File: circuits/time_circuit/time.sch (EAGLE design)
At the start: 6 parts, among them Y2 32.768kHz

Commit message: Integrated wires to main schematic
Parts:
- added GND: SE13, solpad:SE13
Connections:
- net VCC renamed VDD
- net GND: now also GND.MP
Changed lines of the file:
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@@
 <parts>
 <part name="DS1307" library="ds1307_pcf8583" deviceset="DS1307" device=""/>
-<part name="GND1" library="supply1" deviceset="GND" device=""/>
-<part name="GND2" library="supply1" deviceset="GND" device=""/>
-<part name="P+1" library="supply1" deviceset="VCC" device=""/>
 <part name="R1" library="SparkFun-Resistors" deviceset="10KOHM-1/10W-1%(0603)" device="0603" value="10K"/>
 <part name="R2" library="SparkFun-Resistors" deviceset="10KOHM-1/10W-1%(0603)" device="0603" value="10K"/>
-<part name="P+2" library="supply1" deviceset="VCC" device=""/>
-<part name="P+3" library="supply1" deviceset="VCC" device=""/>
 <part name="SCL_RTC" library="solpad" deviceset="SE13" device=""/>
 <part name="SDA_RTC" library="solpad" deviceset="SE13" device=""/>
 <part name="Y2" library="SparkFun-FreqCtrl" deviceset="CRYSTAL" device="TC26H" value="32.768kHz"/>
+<part name="GND" library="solpad" deviceset="SE13" device=""/>
+<part name="GND2" library="supply1" deviceset="GND" device=""/>
+<part name="VDD1" library="supply1" deviceset="VDD" device=""/>
+<part name="VDD2" library="supply1" deviceset="VDD" device=""/>
+<part name="VDD3" library="supply1" deviceset="VDD" device=""/>
 </parts>
 <sheets>
@@
 <instances>
 <instance part="DS1307" gate="G$1" x="48.26" y="60.96"/>
-<instance part="GND1" gate="1" x="33.02" y="53.34" rot="R270"/>
-<instance part="GND2" gate="1" x="63.5" y="53.34" rot="R90"/>
-<instance part="P+1" gate="VCC" x="30.48" y="68.58" rot="R90"/>
 <instance part="R1" gate="G$1" x="60.96" y="76.2" rot="R90"/>
 <instance part="R2" gate="G$1" x="88.9" y="68.58" rot="R90"/>
-<instance part="P+2" gate="VCC" x="60.96" y="83.82"/>
-<instance part="P+3" gate="VCC" x="88.9" y="76.2"/>
 <instance part="SCL_RTC" gate="1" x="73.66" y="68.58" rot="R270"/>
 <instance part="SDA_RTC" gate="1" x="96.52" y="63.5" rot="R270"/>
 <instance part="Y2" gate="G$1" x="22.86" y="60.96" rot="R90"/>
+<instance part="GND" gate="1" x="71.12" y="53.34" rot="R270"/>
+<instance part="GND2" gate="1" x="33.02" y="53.34" rot="R270"/>
+<instance part="VDD1" gate="G$1" x="33.02" y="71.12"/>
+<instance part="VDD2" gate="G$1" x="60.96" y="83.82"/>
+<instance part="VDD3" gate="G$1" x="88.9" y="76.2"/>
 </instances>
 <busses>
 </busses>
 <nets>
-<net name="GND" class="0">
-<segment>
-<pinref part="DS1307" gate="G$1" pin="GND"/>
-<pinref part="GND1" gate="1" pin="GND"/>
-<wire x1="35.56" y1="53.34" x2="38.1" y2="53.34" width="0.1524" layer="91"/>
-</segment>
-<segment>
-<pinref part="DS1307" gate="G$1" pin="VBAT"/>
-<pinref part="GND2" gate="1" pin="GND"/>
-</segment>
-</net>
-<net name="VCC" class="0">
-<segment>
-<pinref part="DS1307" gate="G$1" pin="VCC"/>
-<pinref part="P+1" gate="VCC" pin="VCC"/>
-<wire x1="33.02" y1="68.58" x2="38.1" y2="68.58" width="0.1524" layer="91"/>
-</segment>
-<segment>
-<pinref part="R1" gate="G$1" pin="2"/>
-<pinref part="P+2" gate="VCC" pin="VCC"/>
-</segment>
-<segment>
-<pinref part="R2" gate="G$1" pin="2"/>
-<pinref part="P+3" gate="VCC" pin="VCC"/>
-</segment>
-</net>
 <net name="N$1" class="0">
 <segment>
@@
 </segment>
 </net>
+<net name="GND" class="0">
+<segment>
+<pinref part="DS1307" gate="G$1" pin="GND"/>
+<pinref part="GND2" gate="1" pin="GND"/>
+<wire x1="35.56" y1="53.34" x2="38.1" y2="53.34" width="0.1524" layer="91"/>
+<pinref part="DS1307" gate="G$1" pin="VBAT"/>
+<wire x1="63.5" y1="53.34" x2="60.96" y2="53.34" width="0.1524" layer="91"/>
+<wire x1="38.1" y1="45.72" x2="63.5" y2="45.72" width="0.1524" layer="91"/>
+<wire x1="63.5" y1="45.72" x2="63.5" y2="53.34" width="0.1524" layer="91"/>
+<wire x1="63.5" y1="53.34" x2="68.58" y2="53.34" width="0.1524" layer="91"/>
+<pinref part="GND" gate="1" pin="MP"/>
+<wire x1="38.1" y1="45.72" x2="38.1" y2="53.34" width="0.1524" layer="91"/>
+</segment>
+</net>
+<net name="VDD" class="0">
+<segment>
+<pinref part="DS1307" gate="G$1" pin="VCC"/>
+<wire x1="33.02" y1="68.58" x2="38.1" y2="68.58" width="0.1524" layer="91"/>
+<pinref part="VDD1" gate="G$1" pin="VDD"/>
+</segment>
+<segment>
+<pinref part="R1" gate="G$1" pin="2"/>
+<pinref part="VDD2" gate="G$1" pin="VDD"/>
+</segment>
+<segment>
+<pinref part="R2" gate="G$1" pin="2"/>
+<pinref part="VDD3" gate="G$1" pin="VDD"/>
+</segment>
+</net>

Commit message: Time circuit layout drc
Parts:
- added VDD: SE13, solpad:SE13
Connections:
- net VDD: now also VDD.MP
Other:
- moved on the sheet: GND, R1
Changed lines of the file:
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@@
 <part name="VDD2" library="supply1" deviceset="VDD" device=""/>
 <part name="VDD3" library="supply1" deviceset="VDD" device=""/>
+<part name="VDD" library="solpad" deviceset="SE13" device=""/>
 </parts>
 <sheets>
@@
 <instances>
 <instance part="DS1307" gate="G$1" x="48.26" y="60.96"/>
-<instance part="R1" gate="G$1" x="60.96" y="76.2" rot="R90"/>
+<instance part="R1" gate="G$1" x="63.5" y="76.2" rot="R90"/>
 <instance part="R2" gate="G$1" x="88.9" y="68.58" rot="R90"/>
 <instance part="SCL_RTC" gate="1" x="73.66" y="68.58" rot="R270"/>
 <instance part="SDA_RTC" gate="1" x="96.52" y="63.5" rot="R270"/>
 <instance part="Y2" gate="G$1" x="22.86" y="60.96" rot="R90"/>
-<instance part="GND" gate="1" x="71.12" y="53.34" rot="R270"/>
+<instance part="GND" gate="1" x="68.58" y="53.34" rot="R270"/>
 <instance part="GND2" gate="1" x="33.02" y="53.34" rot="R270"/>
 <instance part="VDD1" gate="G$1" x="33.02" y="71.12"/>
-<instance part="VDD2" gate="G$1" x="60.96" y="83.82"/>
+<instance part="VDD2" gate="G$1" x="63.5" y="83.82"/>
 <instance part="VDD3" gate="G$1" x="88.9" y="76.2"/>
+<instance part="VDD" gate="1" x="35.56" y="71.12"/>
 </instances>
 <busses>
@@
 <segment>
 <pinref part="DS1307" gate="G$1" pin="SCL"/>
+<wire x1="60.96" y1="68.58" x2="63.5" y2="68.58" width="0.1524" layer="91"/>
+<pinref part="SCL_RTC" gate="1" pin="MP"/>
 <pinref part="R1" gate="G$1" pin="1"/>
-<wire x1="60.96" y1="71.12" x2="60.96" y2="68.58" width="0.1524" layer="91"/>
-<wire x1="60.96" y1="68.58" x2="71.12" y2="68.58" width="0.1524" layer="91"/>
-<pinref part="SCL_RTC" gate="1" pin="MP"/>
+<wire x1="63.5" y1="68.58" x2="71.12" y2="68.58" width="0.1524" layer="91"/>
+<wire x1="63.5" y1="71.12" x2="63.5" y2="68.58" width="0.1524" layer="91"/>
 </segment>
 </net>
@@
 <wire x1="38.1" y1="45.72" x2="63.5" y2="45.72" width="0.1524" layer="91"/>
 <wire x1="63.5" y1="45.72" x2="63.5" y2="53.34" width="0.1524" layer="91"/>
-<wire x1="63.5" y1="53.34" x2="68.58" y2="53.34" width="0.1524" layer="91"/>
+<wire x1="63.5" y1="53.34" x2="66.04" y2="53.34" width="0.1524" layer="91"/>
 <pinref part="GND" gate="1" pin="MP"/>
 <wire x1="38.1" y1="45.72" x2="38.1" y2="53.34" width="0.1524" layer="91"/>
@@
 <segment>
 <pinref part="DS1307" gate="G$1" pin="VCC"/>
-<wire x1="33.02" y1="68.58" x2="38.1" y2="68.58" width="0.1524" layer="91"/>
+<wire x1="33.02" y1="68.58" x2="35.56" y2="68.58" width="0.1524" layer="91"/>
 <pinref part="VDD1" gate="G$1" pin="VDD"/>
+<pinref part="VDD" gate="1" pin="MP"/>
+<wire x1="35.56" y1="68.58" x2="38.1" y2="68.58" width="0.1524" layer="91"/>
+<junction x="35.56" y="68.58"/>
 </segment>
 <segment>

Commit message: Update oscillator with SMT part
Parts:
- removed Y2: 32.768kHz, SparkFun-FreqCtrl:CRYSTALTC26H
- added Y1: (no value), SparkFun-FreqCtrl:CRYSTALSMD
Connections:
- net N$3: now also Y1.1; no longer Y2.1
- net N$4: now also Y1.2; no longer Y2.2
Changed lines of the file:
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@@
 <part name="SCL_RTC" library="solpad" deviceset="SE13" device=""/>
 <part name="SDA_RTC" library="solpad" deviceset="SE13" device=""/>
-<part name="Y2" library="SparkFun-FreqCtrl" deviceset="CRYSTAL" device="TC26H" value="32.768kHz"/>
 <part name="GND" library="solpad" deviceset="SE13" device=""/>
 <part name="GND2" library="supply1" deviceset="GND" device=""/>
@@
 <part name="VDD3" library="supply1" deviceset="VDD" device=""/>
 <part name="VDD" library="solpad" deviceset="SE13" device=""/>
+<part name="Y1" library="SparkFun-FreqCtrl" deviceset="CRYSTAL" device="SMD"/>
 </parts>
 <sheets>
@@
 <instance part="SCL_RTC" gate="1" x="73.66" y="68.58" rot="R270"/>
 <instance part="SDA_RTC" gate="1" x="96.52" y="63.5" rot="R270"/>
-<instance part="Y2" gate="G$1" x="22.86" y="60.96" rot="R90"/>
 <instance part="GND" gate="1" x="68.58" y="53.34" rot="R270"/>
 <instance part="GND2" gate="1" x="33.02" y="53.34" rot="R270"/>
@@
 <instance part="VDD3" gate="G$1" x="88.9" y="76.2"/>
 <instance part="VDD" gate="1" x="35.56" y="71.12"/>
+<instance part="Y1" gate="G$1" x="22.86" y="60.96" rot="R90"/>
 </instances>
 <busses>
@@
 <net name="N$3" class="0">
 <segment>
-<pinref part="Y2" gate="G$1" pin="1"/>
 <pinref part="DS1307" gate="G$1" pin="X2"/>
 <wire x1="22.86" y1="58.42" x2="38.1" y2="58.42" width="0.1524" layer="91"/>
+<pinref part="Y1" gate="G$1" pin="1"/>
 </segment>
 </net>
@@
 <segment>
 <pinref part="DS1307" gate="G$1" pin="X1"/>
-<pinref part="Y2" gate="G$1" pin="2"/>
 <wire x1="38.1" y1="63.5" x2="22.86" y2="63.5" width="0.1524" layer="91"/>
+<pinref part="Y1" gate="G$1" pin="2"/>
 </segment>
 </net>

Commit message: time circuit revised
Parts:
- removed DS1307: DS1307, ds1307_pcf8583:DS1307
- added IC1: DS1307Z, ds1307_pcf8583:DS1307Z
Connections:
- net GND: now also IC1.GND, IC1.VBAT; no longer DS1307.GND, DS1307.VBAT
- net N$1: now also IC1.SCL; no longer DS1307.SCL
- net N$2: now also IC1.SDA; no longer DS1307.SDA
- net N$3: now also IC1.X2; no longer DS1307.X2
- net N$4: now also IC1.X1; no longer DS1307.X1
- net VDD: now also IC1.VCC; no longer DS1307.VCC
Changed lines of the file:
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@@
 </classes>
 <parts>
-<part name="DS1307" library="ds1307_pcf8583" deviceset="DS1307" device=""/>
 <part name="R1" library="SparkFun-Resistors" deviceset="10KOHM-1/10W-1%(0603)" device="0603" value="10K"/>
 <part name="R2" library="SparkFun-Resistors" deviceset="10KOHM-1/10W-1%(0603)" device="0603" value="10K"/>
@@
 <part name="VDD" library="solpad" deviceset="SE13" device=""/>
 <part name="Y1" library="SparkFun-FreqCtrl" deviceset="CRYSTAL" device="SMD"/>
+<part name="IC1" library="ds1307_pcf8583" deviceset="DS1307" device="Z"/>
 </parts>
 <sheets>
@@
 </plain>
 <instances>
-<instance part="DS1307" gate="G$1" x="48.26" y="60.96"/>
 <instance part="R1" gate="G$1" x="63.5" y="76.2" rot="R90"/>
 <instance part="R2" gate="G$1" x="88.9" y="68.58" rot="R90"/>
@@
 <instance part="VDD" gate="1" x="35.56" y="71.12"/>
 <instance part="Y1" gate="G$1" x="22.86" y="60.96" rot="R90"/>
+<instance part="IC1" gate="G$1" x="48.26" y="60.96"/>
 </instances>
 <busses>
@@
 <net name="N$1" class="0">
 <segment>
-<pinref part="DS1307" gate="G$1" pin="SCL"/>
 <wire x1="60.96" y1="68.58" x2="63.5" y2="68.58" width="0.1524" layer="91"/>
 <pinref part="SCL_RTC" gate="1" pin="MP"/>
@@
 <wire x1="63.5" y1="68.58" x2="71.12" y2="68.58" width="0.1524" layer="91"/>
 <wire x1="63.5" y1="71.12" x2="63.5" y2="68.58" width="0.1524" layer="91"/>
+<pinref part="IC1" gate="G$1" pin="SCL"/>
 </segment>
 </net>
 <net name="N$2" class="0">
 <segment>
-<pinref part="DS1307" gate="G$1" pin="SDA"/>
 <pinref part="R2" gate="G$1" pin="1"/>
 <wire x1="60.96" y1="63.5" x2="88.9" y2="63.5" width="0.1524" layer="91"/>
@@
 <pinref part="SDA_RTC" gate="1" pin="MP"/>
 <wire x1="93.98" y1="63.5" x2="88.9" y2="63.5" width="0.1524" layer="91"/>
+<pinref part="IC1" gate="G$1" pin="SDA"/>
 </segment>
 </net>
 <net name="N$3" class="0">
 <segment>
-<pinref part="DS1307" gate="G$1" pin="X2"/>
 <wire x1="22.86" y1="58.42" x2="38.1" y2="58.42" width="0.1524" layer="91"/>
 <pinref part="Y1" gate="G$1" pin="1"/>
+<pinref part="IC1" gate="G$1" pin="X2"/>
 </segment>
 </net>
 <net name="N$4" class="0">
 <segment>
-<pinref part="DS1307" gate="G$1" pin="X1"/>
 <wire x1="38.1" y1="63.5" x2="22.86" y2="63.5" width="0.1524" layer="91"/>
 <pinref part="Y1" gate="G$1" pin="2"/>
+<pinref part="IC1" gate="G$1" pin="X1"/>
 </segment>
 </net>
 <net name="GND" class="0">
 <segment>
-<pinref part="DS1307" gate="G$1" pin="GND"/>
 <pinref part="GND2" gate="1" pin="GND"/>
 <wire x1="35.56" y1="53.34" x2="38.1" y2="53.34" width="0.1524" layer="91"/>
-<pinref part="DS1307" gate="G$1" pin="VBAT"/>
 <wire x1="63.5" y1="53.34" x2="60.96" y2="53.34" width="0.1524" layer="91"/>
 <wire x1="38.1" y1="45.72" x2="63.5" y2="45.72" width="0.1524" layer="91"/>
@@
 <pinref part="GND" gate="1" pin="MP"/>
 <wire x1="38.1" y1="45.72" x2="38.1" y2="53.34" width="0.1524" layer="91"/>
+<pinref part="IC1" gate="G$1" pin="VBAT"/>
+<pinref part="IC1" gate="G$1" pin="GND"/>
+<junction x="38.1" y="53.34"/>
 </segment>
 </net>
 <net name="VDD" class="0">
 <segment>
-<pinref part="DS1307" gate="G$1" pin="VCC"/>
 <wire x1="33.02" y1="68.58" x2="35.56" y2="68.58" width="0.1524" layer="91"/>
 <pinref part="VDD1" gate="G$1" pin="VDD"/>
@@
 <wire x1="35.56" y1="68.58" x2="38.1" y2="68.58" width="0.1524" layer="91"/>
 <junction x="35.56" y="68.58"/>
+<pinref part="IC1" gate="G$1" pin="VCC"/>
 </segment>
 <segment>

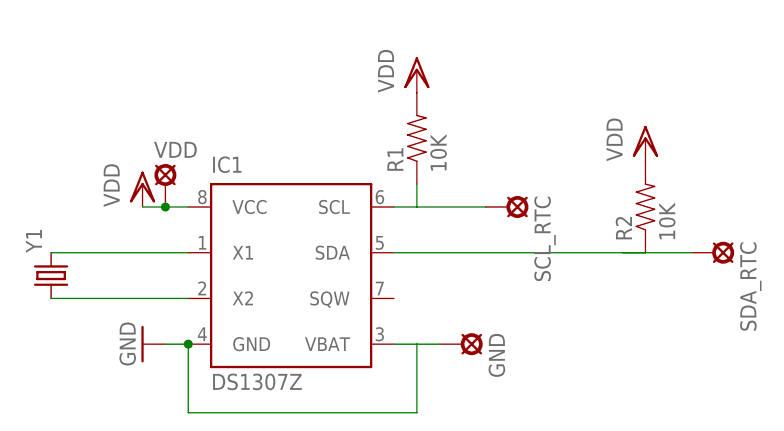
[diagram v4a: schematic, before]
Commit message: Replaced ds1307 with ds1337
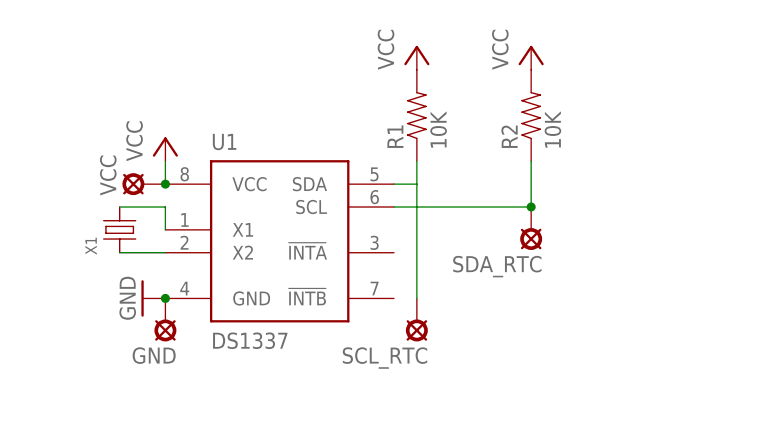
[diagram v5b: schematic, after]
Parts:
- removed IC1: DS1307Z, ds1307_pcf8583:DS1307Z
- removed VDD: SE13, solpad:SE13
- removed Y1: (no value), SparkFun-FreqCtrl:CRYSTALSMD
- added U1: DS1337, ds1337:DS1337
- added VCC: SE13, solpad:SE13
- added X1: (no value), ds1337:CRYSTAL8X3.5MM
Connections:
- removed net VDD: IC1.VCC, R1.2, R2.2, VDD.MP
- new net VCC: R1.2, R2.2, U1.VCC, VCC.MP
- net GND: now also U1.GND; no longer IC1.GND, IC1.VBAT
- net N$1: now also U1.X2, X1.1; no longer IC1.SCL, R1.1, SCL_RTC.MP
- net N$2: now also U1.X1, X1.3; no longer IC1.SDA, R2.1, SDA_RTC.MP
- net N$3: now also R1.1, SCL_RTC.MP, U1.SDA; no longer IC1.X2, Y1.1
- net N$4: now also R2.1, SDA_RTC.MP, U1.SCL; no longer IC1.X1, Y1.2
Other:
- moved on the sheet: GND, R1, R2, SCL_RTC, SDA_RTC
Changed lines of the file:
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@@
 </classes>
 <parts>
+<part name="X1" library="ds1337" deviceset="CRYSTAL" device="8X3.5MM"/>
+<part name="U1" library="ds1337" deviceset="DS1337" device=""/>
+<part name="P+1" library="supply1" deviceset="VCC" device=""/>
+<part name="P+2" library="supply1" deviceset="VCC" device=""/>
+<part name="P+3" library="supply1" deviceset="VCC" device=""/>
 <part name="R1" library="SparkFun-Resistors" deviceset="10KOHM-1/10W-1%(0603)" device="0603" value="10K"/>
 <part name="R2" library="SparkFun-Resistors" deviceset="10KOHM-1/10W-1%(0603)" device="0603" value="10K"/>
+<part name="GND1" library="supply1" deviceset="GND" device=""/>
+<part name="VCC" library="solpad" deviceset="SE13" device=""/>
+<part name="GND" library="solpad" deviceset="SE13" device=""/>
 <part name="SCL_RTC" library="solpad" deviceset="SE13" device=""/>
 <part name="SDA_RTC" library="solpad" deviceset="SE13" device=""/>
-<part name="GND" library="solpad" deviceset="SE13" device=""/>
-<part name="GND2" library="supply1" deviceset="GND" device=""/>
-<part name="VDD1" library="supply1" deviceset="VDD" device=""/>
-<part name="VDD2" library="supply1" deviceset="VDD" device=""/>
-<part name="VDD3" library="supply1" deviceset="VDD" device=""/>
-<part name="VDD" library="solpad" deviceset="SE13" device=""/>
-<part name="Y1" library="SparkFun-FreqCtrl" deviceset="CRYSTAL" device="SMD"/>
-<part name="IC1" library="ds1307_pcf8583" deviceset="DS1307" device="Z"/>
 </parts>
 <sheets>
@@
 </plain>
 <instances>
-<instance part="R1" gate="G$1" x="63.5" y="76.2" rot="R90"/>
-<instance part="R2" gate="G$1" x="88.9" y="68.58" rot="R90"/>
-<instance part="SCL_RTC" gate="1" x="73.66" y="68.58" rot="R270"/>
-<instance part="SDA_RTC" gate="1" x="96.52" y="63.5" rot="R270"/>
-<instance part="GND" gate="1" x="68.58" y="53.34" rot="R270"/>
-<instance part="GND2" gate="1" x="33.02" y="53.34" rot="R270"/>
-<instance part="VDD1" gate="G$1" x="33.02" y="71.12"/>
-<instance part="VDD2" gate="G$1" x="63.5" y="83.82"/>
-<instance part="VDD3" gate="G$1" x="88.9" y="76.2"/>
-<instance part="VDD" gate="1" x="35.56" y="71.12"/>
-<instance part="Y1" gate="G$1" x="22.86" y="60.96" rot="R90"/>
-<instance part="IC1" gate="G$1" x="48.26" y="60.96"/>
+<instance part="X1" gate="G$1" x="30.48" y="66.04" rot="R90"/>
+<instance part="U1" gate="G$1" x="40.64" y="73.66"/>
+<instance part="P+1" gate="VCC" x="35.56" y="76.2"/>
+<instance part="P+2" gate="VCC" x="63.5" y="86.36"/>
+<instance part="P+3" gate="VCC" x="76.2" y="86.36"/>
+<instance part="R1" gate="G$1" x="63.5" y="78.74" rot="R90"/>
+<instance part="R2" gate="G$1" x="76.2" y="78.74" rot="R90"/>
+<instance part="GND1" gate="1" x="33.02" y="58.42" rot="R270"/>
+<instance part="VCC" gate="1" x="33.02" y="71.12" rot="R90"/>
+<instance part="GND" gate="1" x="35.56" y="55.88" rot="R180"/>
+<instance part="SCL_RTC" gate="1" x="63.5" y="55.88" rot="R180"/>
+<instance part="SDA_RTC" gate="1" x="76.2" y="66.04" rot="R180"/>
 </instances>
 <busses>
@@
 <net name="N$1" class="0">
 <segment>
-<wire x1="60.96" y1="68.58" x2="63.5" y2="68.58" width="0.1524" layer="91"/>
-<pinref part="SCL_RTC" gate="1" pin="MP"/>
-<pinref part="R1" gate="G$1" pin="1"/>
-<wire x1="63.5" y1="68.58" x2="71.12" y2="68.58" width="0.1524" layer="91"/>
-<wire x1="63.5" y1="71.12" x2="63.5" y2="68.58" width="0.1524" layer="91"/>
-<pinref part="IC1" gate="G$1" pin="SCL"/>
+<pinref part="X1" gate="G$1" pin="1"/>
+<pinref part="U1" gate="G$1" pin="X2"/>
+<wire x1="30.48" y1="63.5" x2="35.56" y2="63.5" width="0.1524" layer="91"/>
 </segment>
 </net>
 <net name="N$2" class="0">
 <segment>
-<pinref part="R2" gate="G$1" pin="1"/>
-<wire x1="60.96" y1="63.5" x2="88.9" y2="63.5" width="0.1524" layer="91"/>
-<wire x1="88.9" y1="63.5" x2="86.36" y2="63.5" width="0.1524" layer="91"/>
-<pinref part="SDA_RTC" gate="1" pin="MP"/>
-<wire x1="93.98" y1="63.5" x2="88.9" y2="63.5" width="0.1524" layer="91"/>
-<pinref part="IC1" gate="G$1" pin="SDA"/>
+<pinref part="U1" gate="G$1" pin="X1"/>
+<wire x1="35.56" y1="66.04" x2="35.56" y2="68.58" width="0.1524" layer="91"/>
+<pinref part="X1" gate="G$1" pin="3"/>
+<wire x1="35.56" y1="68.58" x2="30.48" y2="68.58" width="0.1524" layer="91"/>
+</segment>
+</net>
+<net name="VCC" class="0">
+<segment>
+<pinref part="U1" gate="G$1" pin="VCC"/>
+<pinref part="P+1" gate="VCC" pin="VCC"/>
+<wire x1="35.56" y1="73.66" x2="35.56" y2="71.12" width="0.1524" layer="91"/>
+<pinref part="VCC" gate="1" pin="MP"/>
+<junction x="35.56" y="71.12"/>
+</segment>
+<segment>
+<pinref part="P+2" gate="VCC" pin="VCC"/>
+<pinref part="R1" gate="G$1" pin="2"/>
+</segment>
+<segment>
+<pinref part="P+3" gate="VCC" pin="VCC"/>
+<pinref part="R2" gate="G$1" pin="2"/>
 </segment>
 </net>
 <net name="N$3" class="0">
 <segment>
-<wire x1="22.86" y1="58.42" x2="38.1" y2="58.42" width="0.1524" layer="91"/>
-<pinref part="Y1" gate="G$1" pin="1"/>
-<pinref part="IC1" gate="G$1" pin="X2"/>
+<pinref part="R1" gate="G$1" pin="1"/>
+<wire x1="63.5" y1="58.42" x2="63.5" y2="71.12" width="0.1524" layer="91"/>
+<pinref part="SCL_RTC" gate="1" pin="MP"/>
+<pinref part="U1" gate="G$1" pin="SDA"/>
+<wire x1="63.5" y1="71.12" x2="63.5" y2="73.66" width="0.1524" layer="91"/>
+<wire x1="60.96" y1="71.12" x2="63.5" y2="71.12" width="0.1524" layer="91"/>
 </segment>
 </net>
 <net name="N$4" class="0">
 <segment>
-<wire x1="38.1" y1="63.5" x2="22.86" y2="63.5" width="0.1524" layer="91"/>
-<pinref part="Y1" gate="G$1" pin="2"/>
-<pinref part="IC1" gate="G$1" pin="X1"/>
+<pinref part="U1" gate="G$1" pin="SCL"/>
+<wire x1="60.96" y1="68.58" x2="76.2" y2="68.58" width="0.1524" layer="91"/>
+<pinref part="R2" gate="G$1" pin="1"/>
+<wire x1="76.2" y1="68.58" x2="76.2" y2="73.66" width="0.1524" layer="91"/>
+<pinref part="SDA_RTC" gate="1" pin="MP"/>
+<junction x="76.2" y="68.58"/>
 </segment>
 </net>
 <net name="GND" class="0">
 <segment>
-<pinref part="GND2" gate="1" pin="GND"/>
-<wire x1="35.56" y1="53.34" x2="38.1" y2="53.34" width="0.1524" layer="91"/>
-<wire x1="63.5" y1="53.34" x2="60.96" y2="53.34" width="0.1524" layer="91"/>
-<wire x1="38.1" y1="45.72" x2="63.5" y2="45.72" width="0.1524" layer="91"/>
-<wire x1="63.5" y1="45.72" x2="63.5" y2="53.34" width="0.1524" layer="91"/>
-<wire x1="63.5" y1="53.34" x2="66.04" y2="53.34" width="0.1524" layer="91"/>
+<pinref part="U1" gate="G$1" pin="GND"/>
+<pinref part="GND1" gate="1" pin="GND"/>
 <pinref part="GND" gate="1" pin="MP"/>
-<wire x1="38.1" y1="45.72" x2="38.1" y2="53.34" width="0.1524" layer="91"/>
-<pinref part="IC1" gate="G$1" pin="VBAT"/>
-<pinref part="IC1" gate="G$1" pin="GND"/>
-<junction x="38.1" y="53.34"/>
+<junction x="35.56" y="58.42"/>
+<pinref part="GND" gate="1" pin="MP"/>
 </segment>
 </net>
-<net name="VDD" class="0">
-<segment>
-<wire x1="33.02" y1="68.58" x2="35.56" y2="68.58" width="0.1524" layer="91"/>
-<pinref part="VDD1" gate="G$1" pin="VDD"/>
-<pinref part="VDD" gate="1" pin="MP"/>
-<wire x1="35.56" y1="68.58" x2="38.1" y2="68.58" width="0.1524" layer="91"/>
-<junction x="35.56" y="68.58"/>
-<pinref part="IC1" gate="G$1" pin="VCC"/>
-</segment>
-<segment>
-<pinref part="R1" gate="G$1" pin="2"/>
-<pinref part="VDD2" gate="G$1" pin="VDD"/>
-</segment>
-<segment>
-<pinref part="R2" gate="G$1" pin="2"/>
-<pinref part="VDD3" gate="G$1" pin="VDD"/>
-</segment>
-</net>
